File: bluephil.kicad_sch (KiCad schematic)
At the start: 1 part, among them U1 STM32WB55CEUx

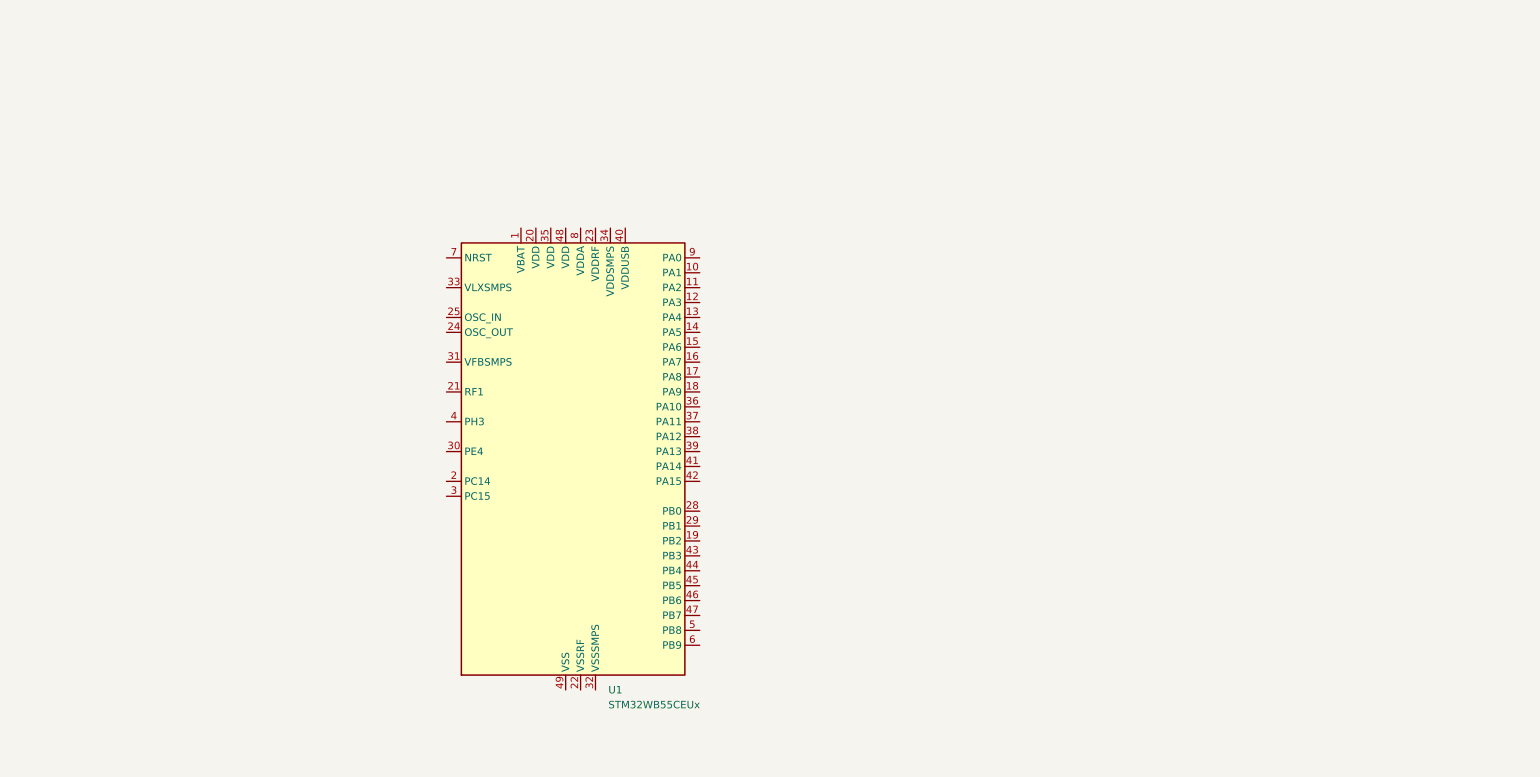
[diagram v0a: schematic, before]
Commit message: Work on Crystals, Bypass Capacitors
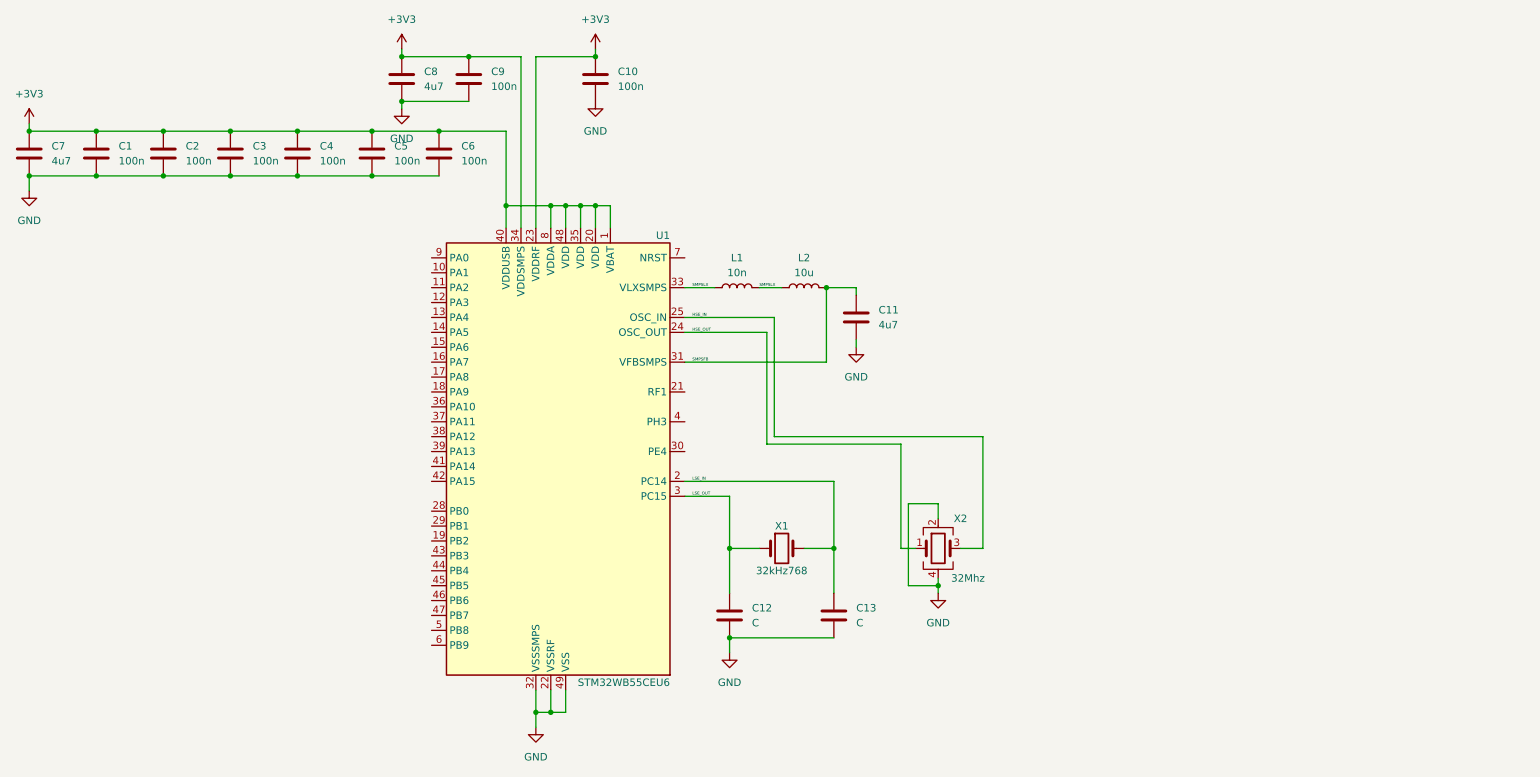
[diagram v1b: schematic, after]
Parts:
- added C1, C10, C2, C3, C4, C5, C6, C9: 100n, symbol Device:C
- added C11, C7, C8: 4u7, symbol Device:C
- added C12, C13: C, symbol Device:C
- added L1: 10n, symbol Device:L
- added L2: 10u, symbol Device:L
- added X1: 32kHz768, symbol Device:Crystal
- added X2: 32Mhz, symbol Device:Crystal_GND24
- U1: value STM32WB55CEUx -> STM32WB55CEU6
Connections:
- net +3V3: now reaches U1.1 (VBAT)
- net +3V3: now also U1.20 (VDD), U1.23 (VDDRF), U1.34 (VDDSMPS), U1.35 (VDD), U1.40 (VDDUSB), U1.48 (VDD), U1.8 (VDDA), C1.1, C10.1, C2.1, C3.1, C4.1, C5.1, C6.1, C7.1, C8.1, C9.1
- net LSE_IN: now reaches U1.2 (PC14)
- net LSE_IN: now also C13.1, X1.2
- net GND: now reaches U1.22 (VSSRF)
- net GND: now also U1.32 (VSSSMPS), U1.49 (VSS), C1.2, C10.2, C11.2, C12.2, C13.2, C2.2, C3.2, C4.2, C5.2, C6.2, C7.2, C8.2, C9.2, X2.2, X2.4
- net HSE_OUT: now reaches U1.24 (OSC_OUT)
- net HSE_OUT: now also X2.1
- net HSE_IN: now reaches U1.25 (OSC_IN)
- net HSE_IN: now also X2.3
- net LSE_OUT: now reaches U1.3 (PC15)
- net LSE_OUT: now also C12.1, X1.1
- net SMPSFB: now reaches U1.31 (VFBSMPS)
- net SMPSFB: now also C11.1, L2.2
- net SMPSLX: now reaches U1.33 (VLXSMPS)
- net SMPSLX: now also L1.1, L1.2, L2.1
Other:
- moved on the sheet: U1

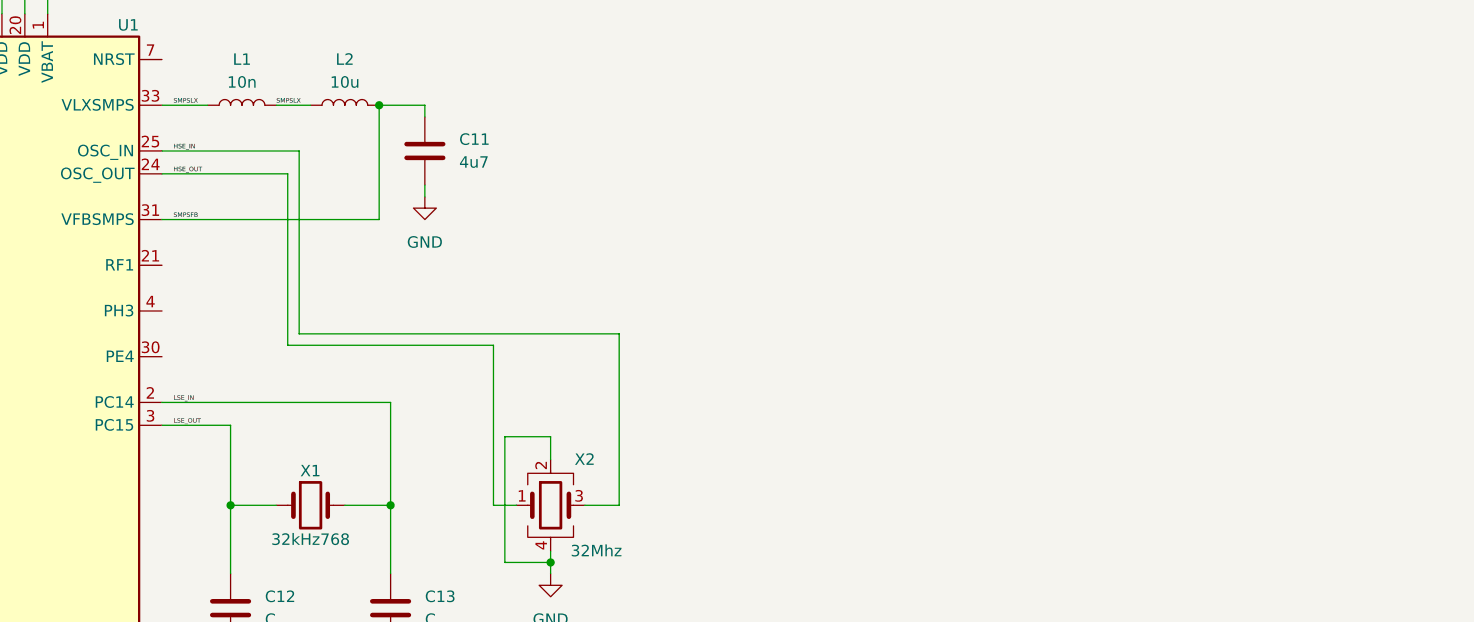
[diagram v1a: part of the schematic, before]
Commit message: added LowPassFilter component
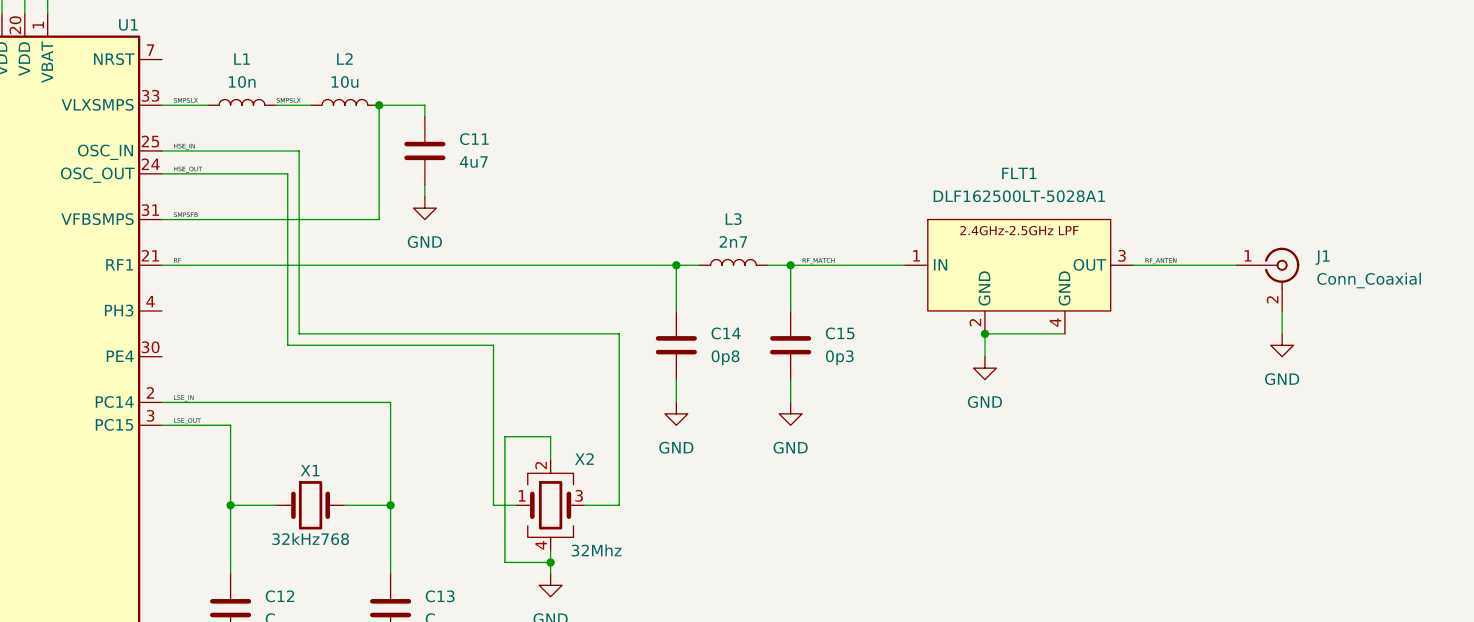
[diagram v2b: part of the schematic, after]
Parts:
- added C14: 0p8, symbol Device:C
- added C15: 0p3, symbol Device:C
- added FLT1: DLF162500LT-5028A1, symbol New_Library:DLF162500LT-5028A1
- added J1: Conn_Coaxial, symbol Connector:Conn_Coaxial
- added L3: 2n7, symbol Device:L
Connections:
- net GND: now also C14.2, C15.2, FLT1.2 (GND), FLT1.4 (GND), J1.2 (Ext)
- net RF: now reaches U1.21 (RF1)
- net RF: now also C14.1, L3.1
- new net RF_ANTEN: FLT1.3 (OUT), J1.1 (In)
- new net RF_MATCH: C15.1, FLT1.1 (IN), L3.2
